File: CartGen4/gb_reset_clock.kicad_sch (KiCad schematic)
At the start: 7 parts, among them U2 SN74LV1T34DCKR

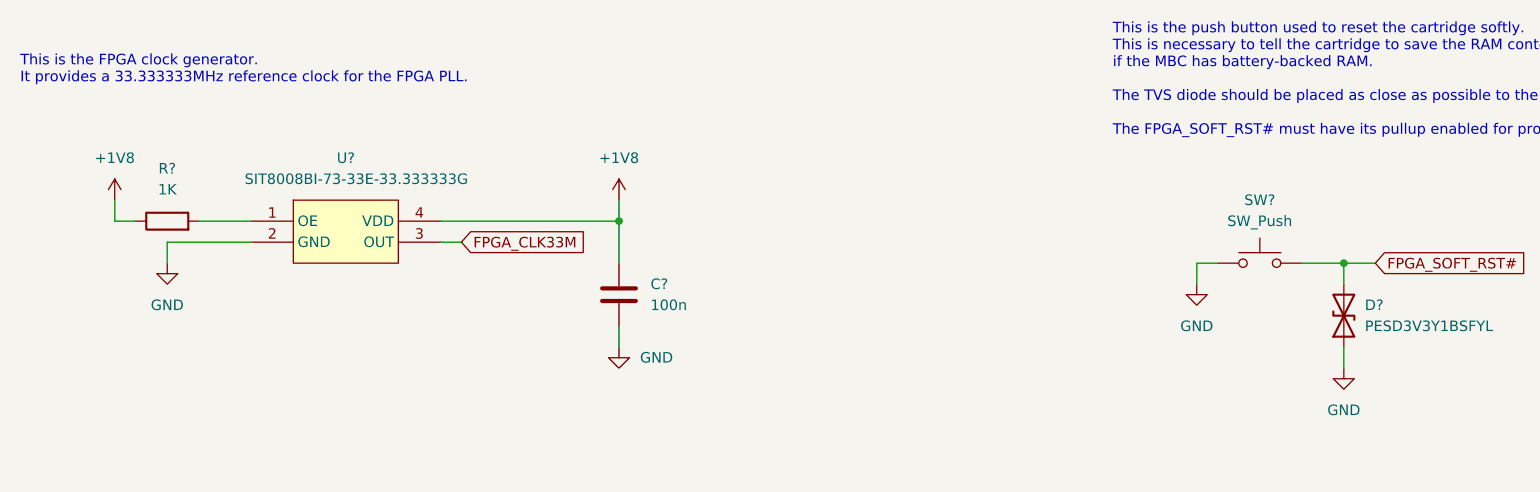
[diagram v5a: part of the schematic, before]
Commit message: Added reference designators to everything
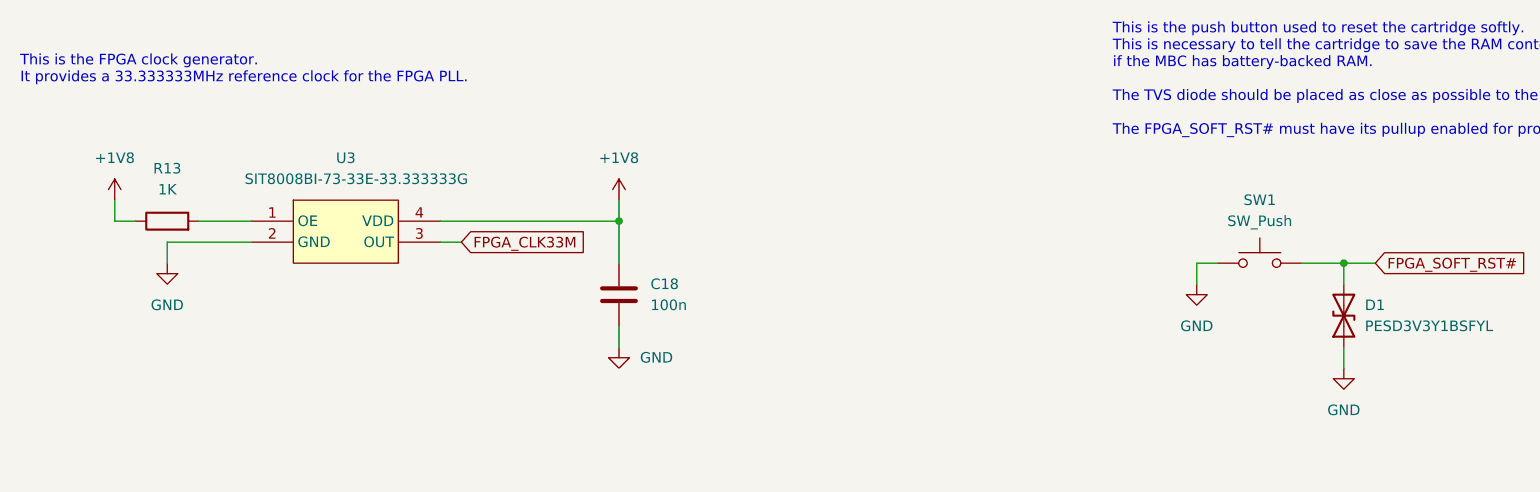
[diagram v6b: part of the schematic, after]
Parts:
- gave numbers to parts that had none: 5
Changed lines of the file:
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@@
   (symbol (lib_id "Device:D_TVS") (at 199.39 72.39 90) (unit 1)
     (in_bom yes) (on_board yes) (fields_autoplaced)
-    (property "Reference" "D?" (id 0) (at 201.93 71.1199 90)
+    (property "Reference" "D1" (id 0) (at 201.93 71.1199 90)
       (effects (font (size 1.27 1.27)) (justify right))
     )
@@
   (symbol (lib_id "power:GND") (at 57.15 66.04 0) (unit 1)
     (in_bom yes) (on_board yes) (fields_autoplaced)
-    (property "Reference" "#PWR?" (id 0) (at 57.15 72.39 0)
+    (property "Reference" "#PWR032" (id 0) (at 57.15 72.39 0)
       (effects (font (size 1.27 1.27)) hide)
     )
@@
   (symbol (lib_id "Device:R") (at 57.15 60.96 90) (unit 1)
     (in_bom yes) (on_board yes) (fields_autoplaced)
-    (property "Reference" "R?" (id 0) (at 57.15 54.61 90))
+    (property "Reference" "R13" (id 0) (at 57.15 54.61 90))
     (property "Value" "1K" (id 1) (at 57.15 57.15 90))
     (property "Footprint" "" (id 2) (at 57.15 62.738 90)
@@
   (symbol (lib_id "power:+1V8") (at 50.8 58.42 0) (unit 1)
     (in_bom yes) (on_board yes) (fields_autoplaced)
-    (property "Reference" "#PWR?" (id 0) (at 50.8 62.23 0)
+    (property "Reference" "#PWR031" (id 0) (at 50.8 62.23 0)
       (effects (font (size 1.27 1.27)) hide)
     )
@@
   (symbol (lib_id "power:GND") (at 181.61 68.58 0) (unit 1)
     (in_bom yes) (on_board yes) (fields_autoplaced)
-    (property "Reference" "#PWR?" (id 0) (at 181.61 74.93 0)
+    (property "Reference" "#PWR036" (id 0) (at 181.61 74.93 0)
       (effects (font (size 1.27 1.27)) hide)
     )
@@
   (symbol (lib_id "SamacSys_Parts:SIT8008BI-73-33E-33.333333G") (at 72.39 58.42 0) (unit 1)
     (in_bom yes) (on_board yes)
-    (property "Reference" "U?" (id 0) (at 78.74 53.34 0))
+    (property "Reference" "U3" (id 0) (at 78.74 53.34 0))
     (property "Value" "SIT8008BI-73-33E-33.333333G" (id 1) (at 80.01 55.88 0))
     (property "Footprint" "" (id 2) (at 72.39 58.42 0)
@@
   (symbol (lib_id "power:+5V") (at 119.38 118.11 0) (unit 1)
     (in_bom yes) (on_board yes) (fields_autoplaced)
-    (property "Reference" "#PWR?" (id 0) (at 119.38 121.92 0)
+    (property "Reference" "#PWR035" (id 0) (at 119.38 121.92 0)
       (effects (font (size 1.27 1.27)) hide)
     )
@@
   (symbol (lib_id "Switch:SW_Push") (at 189.23 66.04 0) (unit 1)
     (in_bom yes) (on_board yes) (fields_autoplaced)
-    (property "Reference" "SW?" (id 0) (at 189.23 58.42 0))
+    (property "Reference" "SW1" (id 0) (at 189.23 58.42 0))
     (property "Value" "SW_Push" (id 1) (at 189.23 60.96 0))
     (property "Footprint" "" (id 2) (at 189.23 60.96 0)
@@
   (symbol (lib_id "power:GND") (at 199.39 78.74 0) (unit 1)
     (in_bom yes) (on_board yes) (fields_autoplaced)
-    (property "Reference" "#PWR?" (id 0) (at 199.39 85.09 0)
+    (property "Reference" "#PWR037" (id 0) (at 199.39 85.09 0)
       (effects (font (size 1.27 1.27)) hide)
     )
@@
   (symbol (lib_id "Device:C") (at 111.76 69.85 0) (unit 1)
     (in_bom yes) (on_board yes) (fields_autoplaced)
-    (property "Reference" "C?" (id 0) (at 115.57 68.5799 0)
+    (property "Reference" "C18" (id 0) (at 115.57 68.5799 0)
       (effects (font (size 1.27 1.27)) (justify left))
     )
@@
   (symbol (lib_id "power:GND") (at 111.76 76.2 0) (unit 1)
     (in_bom yes) (on_board yes) (fields_autoplaced)
-    (property "Reference" "#PWR?" (id 0) (at 111.76 82.55 0)
+    (property "Reference" "#PWR034" (id 0) (at 111.76 82.55 0)
       (effects (font (size 1.27 1.27)) hide)
     )
@@
   (symbol (lib_id "power:+1V8") (at 111.76 58.42 0) (unit 1)
     (in_bom yes) (on_board yes) (fields_autoplaced)
-    (property "Reference" "#PWR?" (id 0) (at 111.76 62.23 0)
-      (effects (font (size 1.27 1.27)) hide)
-    )
+    (property "Reference" "#PWR033" (id 0) (at 111.76 62.23 0)
+      (effects (font (size 1.27 1.27)) hide)
+    )

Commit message: Cleaned up symbol fields
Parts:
- U2: Height 1.1 -> (none); MFN (none) -> Texas Instruments; MFP (none) -> SN74LV1T34DCKR; Manufacturer_Name Texas Instruments -> (none); Manufacturer_Part_Number SN74LV1T34DCKR -> (none); Mouser Part Number 595-SN74LV1T34DCKR -> (none); Mouser Price/Stock https://www.mouser.co.uk/ProductDetail/Texas-Instruments/SN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 -> (none)
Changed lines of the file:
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@@
       (effects (font (size 1.27 1.27)) (justify left) hide)
     )
-    (property "Height" "1.1" (id 5) (at 87.63 123.19 0)
+    (property "MFN" "Texas Instruments" (id 5) (at 87.63 130.81 0)
       (effects (font (size 1.27 1.27)) (justify left) hide)
     )
-    (property "Mouser Part Number" "595-SN74LV1T34DCKR" (id 6) (at 87.63 125.73 0)
+    (property "MFP" "SN74LV1T34DCKR" (id 6) (at 87.63 133.35 0)
       (effects (font (size 1.27 1.27)) (justify left) hide)
     )
-    (property "Mouser Price/Stock" "https://www.mouser.co.uk/ProductDetail/Texas-Instruments/SN74LV1T34DCKR?qs=8sOby8ZxZLGjFfifrzzjkQ%3D%3D" (id 7) (at 87.63 128.27 0)
-      (effects (font (size 1.27 1.27)) (justify left) hide)
-    )
-    (property "Manufacturer_Name" "Texas Instruments" (id 8) (at 87.63 130.81 0)
-      (effects (font (size 1.27 1.27)) (justify left) hide)
-    )
-    (property "Manufacturer_Part_Number" "SN74LV1T34DCKR" (id 9) (at 87.63 133.35 0)
-      (effects (font (size 1.27 1.27)) (justify left) hide)
-    )

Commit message: Added symbol information to obvious stuff
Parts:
- C18: Critical (none) -> N; Notes (none) -> Bypass capacitor for PWR/GND coupling.
- D1: Critical (none) -> N; Notes (none) -> ESD protection for exposed reset button.
- U2: Critical (none) -> Y; Notes (none) -> Used for voltage conversion between FPGA and Gameboy reset; Package ID (none) -> SC70-5; Source (none) -> SPEC
- U3: Critical (none) -> Y; MFN (none) -> SiTime; MFP (none) -> SIT8008BI-73-33E-33.333333G; Notes (none) -> Used for FPGA reference clock.; Source (none) -> SPEC
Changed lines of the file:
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@@
+      (effects (font (size 1.27 1.27)) hide)
+    )
+    (property "Critical" "N" (id 4) (at 199.39 72.39 0)
+      (effects (font (size 1.27 1.27)) hide)
+    )
+    (property "Notes" "ESD protection for exposed reset button." (id 5) (at 199.39 72.39 0)
       (effects (font (size 1.27 1.27)) hide)
     )
@@
       (effects (font (size 1.27 1.27)) (justify left) hide)
     )
+    (property "Notes" "Used for voltage conversion between FPGA and Gameboy reset" (id 7) (at 66.04 118.11 0)
+      (effects (font (size 1.27 1.27)) hide)
+    )
+    (property "Package ID" "SC70-5" (id 8) (at 66.04 118.11 0)
+      (effects (font (size 1.27 1.27)) hide)
+    )
+    (property "Source" "SPEC" (id 9) (at 66.04 118.11 0)
+      (effects (font (size 1.27 1.27)) hide)
+    )
+    (property "Critical" "Y" (id 10) (at 66.04 118.11 0)
+      (effects (font (size 1.27 1.27)) hide)
+    )
     (pin "1")
     (pin "2")
@@
       (effects (font (size 1.27 1.27)) hide)
     )
+    (property "Description" "Standard Clock Oscillators -40 to 85C, 2016, 50ppm, 3.3V, 33.333333MHz, OE, 250 pcs T&R 8 mm" (id 4) (at 72.39 58.42 0)
+      (effects (font (size 1.27 1.27)) hide)
+    )
+    (property "MFN" "SiTime" (id 5) (at 72.39 58.42 0)
+      (effects (font (size 1.27 1.27)) hide)
+    )
+    (property "MFP" "SIT8008BI-73-33E-33.333333G" (id 6) (at 72.39 58.42 0)
+      (effects (font (size 1.27 1.27)) hide)
+    )
+    (property "Notes" "Used for FPGA reference clock." (id 7) (at 72.39 58.42 0)
+      (effects (font (size 1.27 1.27)) hide)
+    )
+    (property "Package ID" "~" (id 8) (at 72.39 58.42 0)
+      (effects (font (size 1.27 1.27)) hide)
+    )
+    (property "Source" "SPEC" (id 9) (at 72.39 58.42 0)
+      (effects (font (size 1.27 1.27)) hide)
+    )
+    (property "Critical" "Y" (id 10) (at 72.39 58.42 0)
+      (effects (font (size 1.27 1.27)) hide)
+    )
     (pin "1")
     (pin "2")
@@
       (effects (font (size 1.27 1.27)) hide)
     )
+    (property "Critical" "N" (id 4) (at 111.76 69.85 0)
+      (effects (font (size 1.27 1.27)) hide)
+    )
+    (property "Notes" "Bypass capacitor for PWR/GND coupling." (id 5) (at 111.76 69.85 0)
+      (effects (font (size 1.27 1.27)) hide)
+    )
